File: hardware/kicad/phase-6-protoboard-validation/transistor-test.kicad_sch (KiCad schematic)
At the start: 5 parts, among them Q1 2N3904

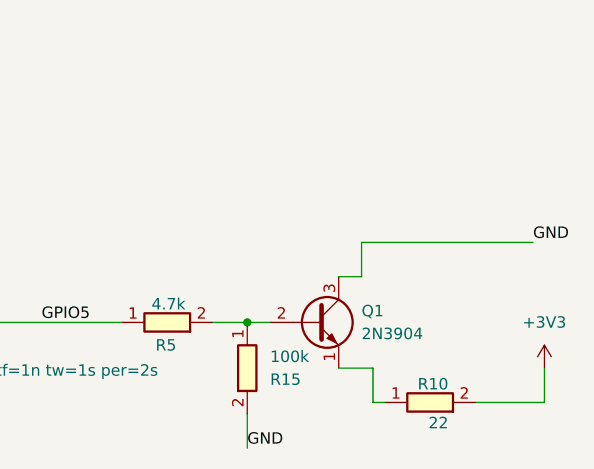
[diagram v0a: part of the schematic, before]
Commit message: Update phase 6 and simulation
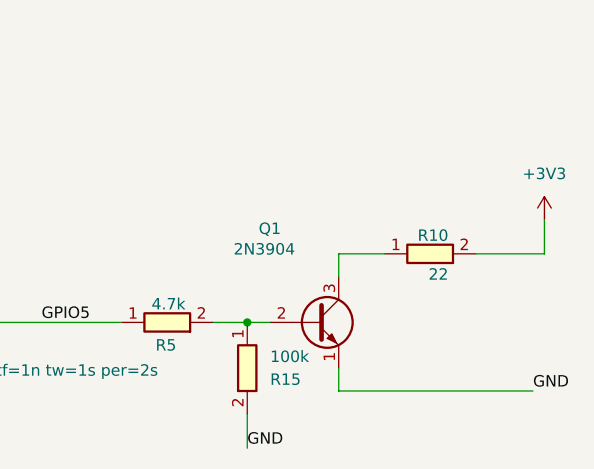
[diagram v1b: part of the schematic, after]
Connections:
- net GND: now also Q1.1 (E); no longer Q1.3 (C)
- net at R10.1: now also Q1.3 (C); no longer Q1.1 (E)
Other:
- moved on the sheet: R10
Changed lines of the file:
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@@
+	(wire
+		(pts
+			(xy 135.89 91.44) (xy 135.89 93.98)
+		)
+		(stroke
+			(width 0)
+			(type default)
+		)
+	)
 	(wire
 		(pts
@@
 	(wire
 		(pts
-			(xy 139.7 107.95) (xy 139.7 104.14)
-		)
-		(stroke
-			(width 0)
-			(type default)
-		)
-	)
-	(wire
-		(pts
-			(xy 138.43 90.17) (xy 138.43 93.98)
-		)
-		(stroke
-			(width 0)
-			(type default)
-		)
-	)
-	(wire
-		(pts
-			(xy 140.97 107.95) (xy 139.7 107.95)
-		)
-		(stroke
-			(width 0)
-			(type default)
-		)
-	)
-	(wire
-		(pts
-			(xy 158.75 107.95) (xy 158.75 104.14)
-		)
-		(stroke
-			(width 0)
-			(type default)
-		)
-	)
-	(wire
-		(pts
-			(xy 151.13 107.95) (xy 158.75 107.95)
+			(xy 158.75 91.44) (xy 158.75 87.63)
+		)
+		(stroke
+			(width 0)
+			(type default)
+		)
+	)
+	(wire
+		(pts
+			(xy 151.13 91.44) (xy 158.75 91.44)
+		)
+		(stroke
+			(width 0)
+			(type default)
+		)
+	)
+	(wire
+		(pts
+			(xy 135.89 106.68) (xy 135.89 104.14)
 		)
 		(stroke
@@
 	(wire
 		(pts
-			(xy 157.48 90.17) (xy 138.43 90.17)
-		)
-		(stroke
-			(width 0)
-			(type default)
-		)
-	)
-	(wire
-		(pts
 			(xy 121.92 99.06) (xy 125.73 99.06)
 		)
@@
 	(wire
 		(pts
-			(xy 138.43 93.98) (xy 135.89 93.98)
+			(xy 135.89 106.68) (xy 157.48 106.68)
 		)
 		(stroke
@@
 	(wire
 		(pts
-			(xy 139.7 104.14) (xy 135.89 104.14)
+			(xy 135.89 91.44) (xy 140.97 91.44)
 		)
 		(stroke
@@
 	)
 	(label ""
-		(at 152.4 107.95 0)
+		(at 152.4 91.44 0)
 		(fields_autoplaced yes)
 		(effects
@@
 		)
 		(property "R10_P2" ""
-			(at 152.4 109.22 0)
+			(at 152.4 92.71 0)
 			(show_name yes)
 			(do_not_autoplace no)
@@
 	)
 	(label "GND"
-		(at 157.48 90.17 0)
+		(at 157.48 106.68 0)
 		(effects
 			(font
@@
 	(symbol
 		(lib_id "power:+3V3")
-		(at 158.75 104.14 0)
+		(at 158.75 87.63 0)
 		(unit 1)
 		(body_style 1)
@@
 		(fields_autoplaced yes)
 		(property "Reference" "#PWR01"
-			(at 158.75 107.95 0)
+			(at 158.75 91.44 0)
 			(hide yes)
 			(show_name no)
@@
 		)
 		(property "Value" "+3V3"
-			(at 158.75 99.06 0)
+			(at 158.75 82.55 0)
 			(show_name no)
 			(do_not_autoplace no)
@@
 		)
 		(property "Footprint" ""
-			(at 158.75 104.14 0)
+			(at 158.75 87.63 0)
 			(hide yes)
 			(show_name no)
@@
 		)
 		(property "Datasheet" ""
-			(at 158.75 104.14 0)
+			(at 158.75 87.63 0)
 			(hide yes)
 			(show_name no)
@@
 		)
 		(property "Description" "Power symbol creates a global label with name \"+3V3\""
-			(at 158.75 104.14 0)
+			(at 158.75 87.63 0)
 			(hide yes)
 			(show_name no)
@@
 		(in_pos_files yes)
 		(dnp no)
-		(fields_autoplaced yes)
 		(property "Reference" "Q1"
-			(at 138.43 97.7899 0)
+			(at 127 88.646 0)
 			(show_name no)
 			(do_not_autoplace no)
@@
 		)
 		(property "Value" "2N3904"
-			(at 138.43 100.3299 0)
+			(at 124.206 90.932 0)
 			(show_name no)
 			(do_not_autoplace no)
@@
 	(symbol
 		(lib_id "Phase6:R")
-		(at 146.05 107.95 90)
+		(at 146.05 91.44 90)
 		(unit 1)
 		(body_style 1)
@@
 		(dnp no)
 		(property "Reference" "R10"
-			(at 148.082 105.918 90)
+			(at 148.082 89.408 90)
 			(show_name no)
 			(do_not_autoplace no)
@@
 		)
 		(property "Value" "22"
-			(at 148.082 110.236 90)
+			(at 148.082 93.726 90)
 			(show_name no)
 			(do_not_autoplace no)
@@
 		)
 		(property "Footprint" "Resistor_THT:R_Axial_DIN0207_L6.3mm_D2.5mm_P7.62mm_Horizontal"
-			(at 146.05 107.95 90)
+			(at 146.05 91.44 90)
 			(hide yes)
 			(show_name no)
@@
 		)
 		(property "Datasheet" "~"
-			(at 146.05 107.95 90)
+			(at 146.05 91.44 90)
 			(hide yes)
 			(show_name no)
@@
 		)
 		(property "Description" "CENTER action resistor"
-			(at 146.05 107.95 90)
-			(hide yes)
-			(show_name no)
+			(at 146.05 91.44 90)
+			(hide yes)
+			(show_name no)
